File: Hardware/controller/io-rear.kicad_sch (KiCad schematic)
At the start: 44 parts

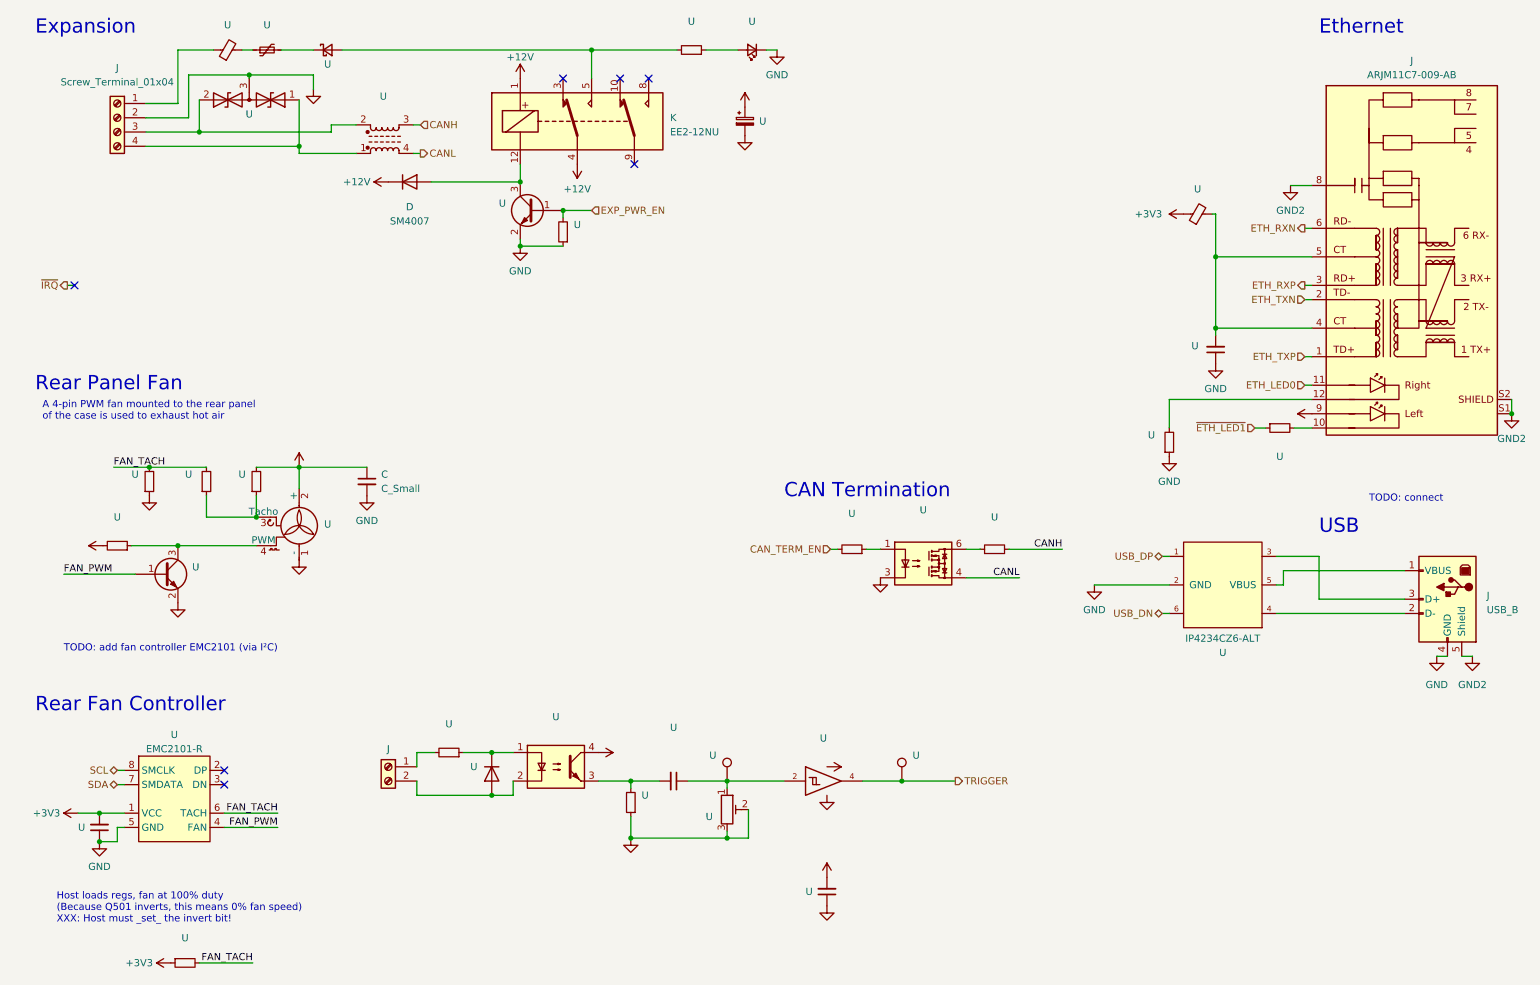
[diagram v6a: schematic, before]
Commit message: hw: add more part numbers, cleanup
- Added JLCPCB part numbers for more passive components

- Added a status LED for the rear of the board (next to the device USB
  port)
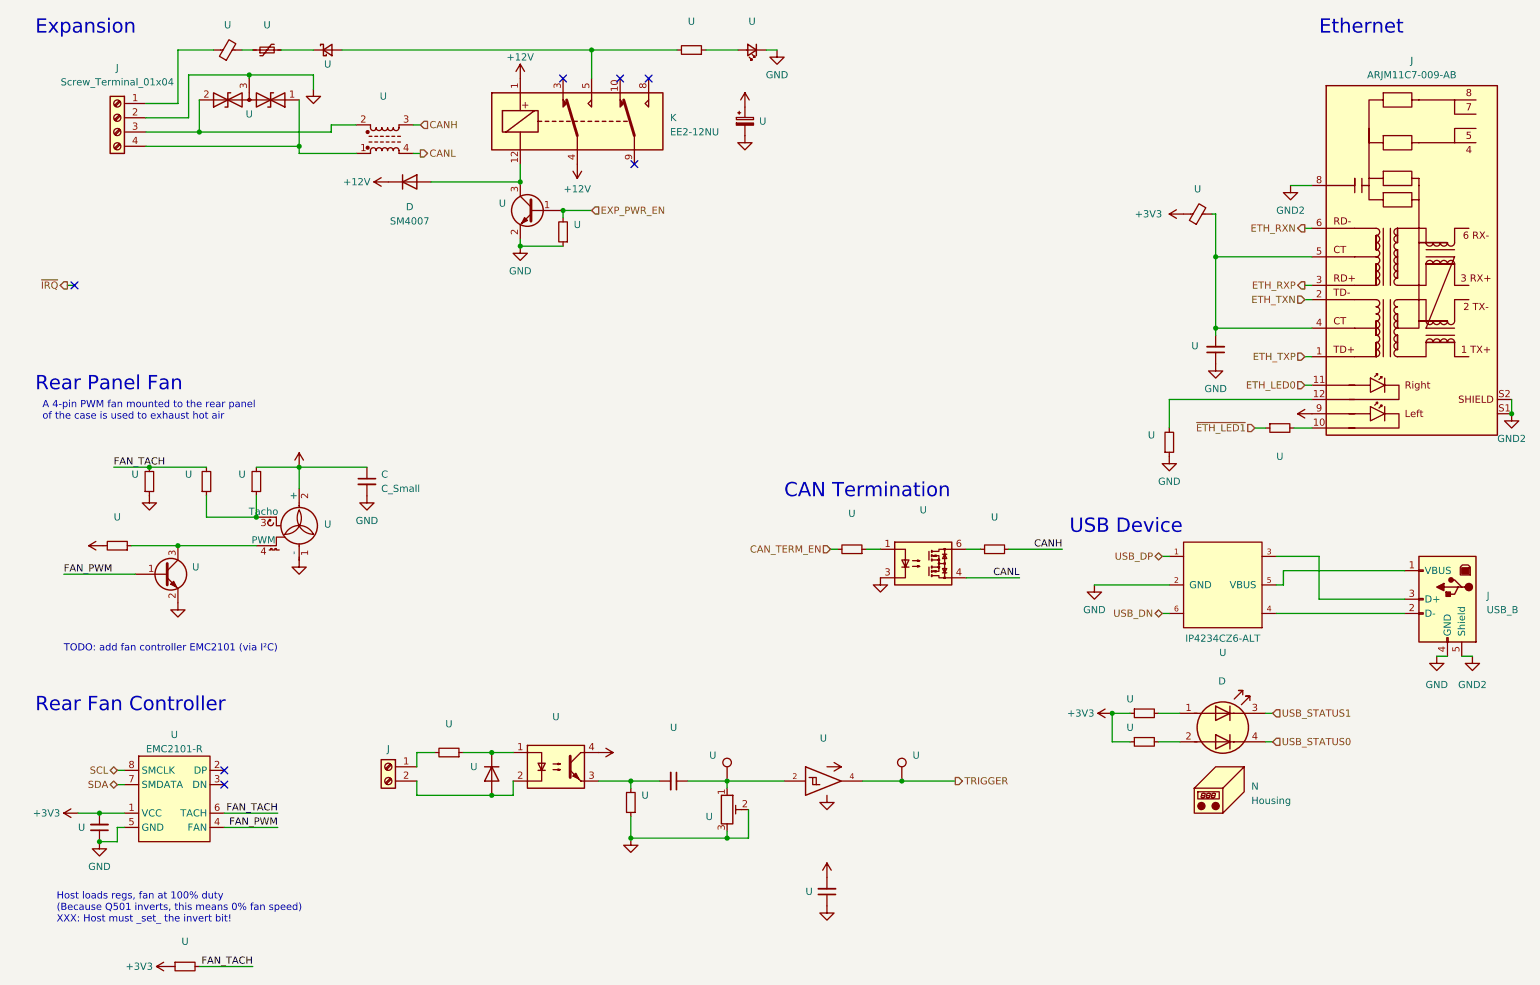
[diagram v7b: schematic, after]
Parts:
- added D: LED_Dual_AAKK, symbol Device:LED_Dual_AAKK
- added N: Housing, symbol Mechanical:Housing
- added U (x2): (no value), symbol Device:R_Small
- U: JLCPCB (none) -> C14663
- U: JLCPCB (none) -> C22775
- U: JLCPCB (none) -> C2297
- U: JLCPCB (none) -> C21190
- U: JLCPCB (none) -> C25819
- U: JLCPCB (none) -> C20526
- U: JLCPCB (none) -> C23162
- U: JLCPCB (none) -> C8218
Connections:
- net +3V3: now also U.1, U.1
- new net: D.2 (A2), U.2
- new net: D.1 (A1), U.2
- new net USB_STATUS0: D.4 (K2)
- new net USB_STATUS1: D.3 (K1)
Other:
- note added: "USB Device"
- note removed: "TODO: connect"
- note removed: "USB"
- moved on the sheet: U

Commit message: hw: fix part numbers
- fixed missing or incorrect MPN and JLCPCB part numbers for various
  components; most should have either one of these now
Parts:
- C: JLCPCB (none) -> C15850; JLPCB C15850 -> (none)
- N: MPN (none) -> SLP3-150-300-F
- U: MPN (none) -> IP4234CZ6,125
- U: JLCPCB (none) -> C23162
- U: JLCPCB (none) -> C1015
- U: JLCPCB (none) -> C81598
- U: MPN (none) -> WR06X2742FTL
- U: MPN (none) -> EMC2101-R-ACZL-TR
- U: JLCPCB (none) -> C15849; MPN (none) -> CL10B105KP8NFNC
- U: JLCPCB (none) -> C21122
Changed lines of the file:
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@@
       (effects (font (size 1.27 1.27)) (justify right) hide)
+    )
+    (property "MPN" "IP4234CZ6,125" (id 4) (at 237.49 124.46 0)
+      (effects (font (size 1.27 1.27)) hide)
     )
     (pin "1")
@@
       (effects (font (size 1.27 1.27)) hide)
     )
+    (property "JLCPCB" "C23162" (id 4) (at 113.03 53.975 0)
+      (effects (font (size 1.27 1.27)) hide)
+    )
     (pin "1")
     (pin "2")
@@
       (effects (font (size 1.27 1.27)) hide)
     )
+    (property "MPN" "SLP3-150-300-F" (id 4) (at 231.14 153.035 0)
+      (effects (font (size 1.27 1.27)) hide)
+    )
   )
   (symbol (lib_id "Device:D_Schottky_Small") (at 71.12 21.59 0) (unit 1)
@@
     )
     (property "MPN" "MFBM1V2012-800-R" (id 4) (at 226.06 50.8 90)
+      (effects (font (size 1.27 1.27)) hide)
+    )
+    (property "JLCPCB" "C1015" (id 5) (at 226.06 50.8 90)
       (effects (font (size 1.27 1.27)) hide)
     )
@@
       (effects (font (size 1.27 1.27)) hide)
     )
-    (property "JLPCB" "C15850" (id 4) (at 78.105 98.425 0)
+    (property "JLCPCB" "C15850" (id 4) (at 78.105 98.425 0)
       (effects (font (size 1.27 1.27)) hide)
     )
@@
       (effects (font (size 1.27 1.27)) hide)
     )
+    (property "JLCPCB" "C81598" (id 5) (at 100.33 150.495 90)
+      (effects (font (size 1.27 1.27)) hide)
+    )
     (pin "1")
     (pin "2")
@@
     )
     (property "Datasheet" "~" (id 3) (at 49.53 98.425 0)
+      (effects (font (size 1.27 1.27)) hide)
+    )
+    (property "MPN" "WR06X2742FTL" (id 4) (at 49.53 98.425 0)
       (effects (font (size 1.27 1.27)) hide)
     )
@@
     )
     (property "Datasheet" "https://ww1.microchip.com/downloads/en/DeviceDoc/2101.pdf" (id 3) (at 43.815 140.97 0)
+      (effects (font (size 1.27 1.27)) hide)
+    )
+    (property "MPN" "EMC2101-R-ACZL-TR" (id 4) (at 43.815 147.32 0)
       (effects (font (size 1.27 1.27)) hide)
     )
@@
       (effects (font (size 1.27 1.27)) hide)
     )
-    (property "MPN" "" (id 4) (at 132.715 151.765 0)
+    (property "MPN" "CL10B105KP8NFNC" (id 4) (at 132.715 151.765 0)
+      (effects (font (size 1.27 1.27)) hide)
+    )
+    (property "JLCPCB" "C15849" (id 5) (at 132.715 151.765 90)
       (effects (font (size 1.27 1.27)) hide)
     )
@@
       (effects (font (size 1.27 1.27)) hide)
     )
+    (property "JLCPCB" "C21122" (id 5) (at 229.235 74.93 0)
+      (effects (font (size 1.27 1.27)) hide)
+    )
     (pin "1")
     (pin "2")
@@
       (effects (font (size 1.27 1.27)) hide)
     )
+    (property "JLCPCB" "C1015" (id 5) (at 53.34 21.59 90)
+      (effects (font (size 1.27 1.27)) hide)
+    )
